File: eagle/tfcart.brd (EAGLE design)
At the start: 71.9 x 55.5 mm, 19 parts, among them CN1 MSX_CART, IC7 AT27C020-55JUPLCCS32, IC8 LM1117MPX-3.3

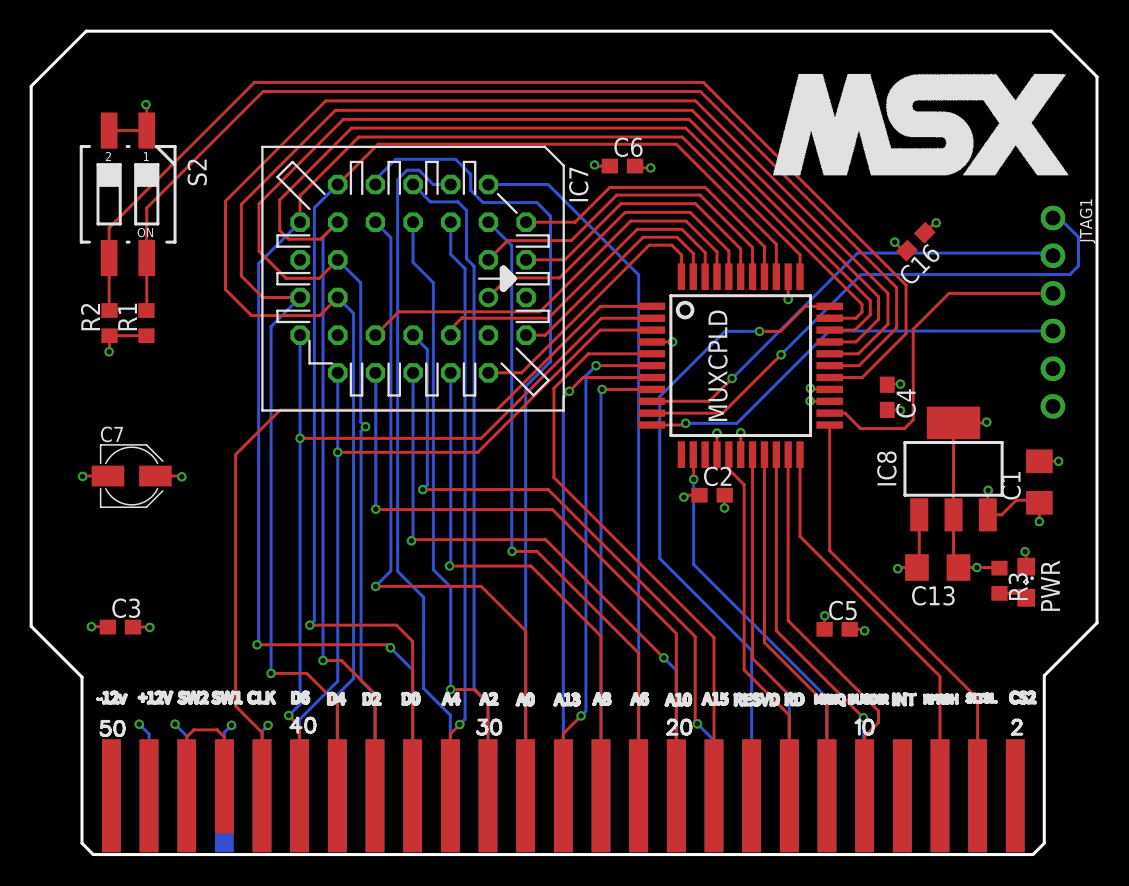
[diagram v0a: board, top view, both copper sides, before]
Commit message: MSX Cartridge v1.0 - Complete CPLD-based MegaROM implementation
A minimalist MSX cartridge design based on Xilinx XC9536XL CPLD with
complete build automation and manufacturing outputs.

NOTE: This project has been superseded by RISKYMSX. For new builds,
please use https://github.com/arkadiuszmakarenko/RISKYMSX which offers
superior features including USB ROM loading, SCC emulation, and better
user experience.

Features:
- Xilinx XC9536XL CPLD implementing standard MegaROM mapper
- 4 switchable ROM pages (8KB each) for up to 512KB ROMs
- Docker-based automated build system
- Complete PCB manufacturing pipeline (Gerbers, BOM, CPL, PDF)
- GitHub Actions CI/CD workflows
- GPL v3 licensed hardware and HDL

Build System:
- Docker containers for reproducible builds
- Automated firmware compilation with git versioning
- Eagle CAM processing for PCB manufacturing
- BOM/CPL extraction for assembly
- Automated release packaging

GitHub Actions Workflows:
- Firmware build (CPLD synthesis)
- Gerber generation (PCB fabrication files)
- Assembly file generation (BOM and CPL)
- Schematic PDF generation
- Complete release packaging

Manufacturing:
- 4-layer PCB design optimized for JLCPCB
- Automated Gerber generation via Eagle CAM
- Python scripts for BOM/CPL extraction
- Complete documentation for assembly

License: GNU General Public License v3.0
Copyright (C) 2021-2025 Stephen J. Leary

Build system based on tf536_public project structure.
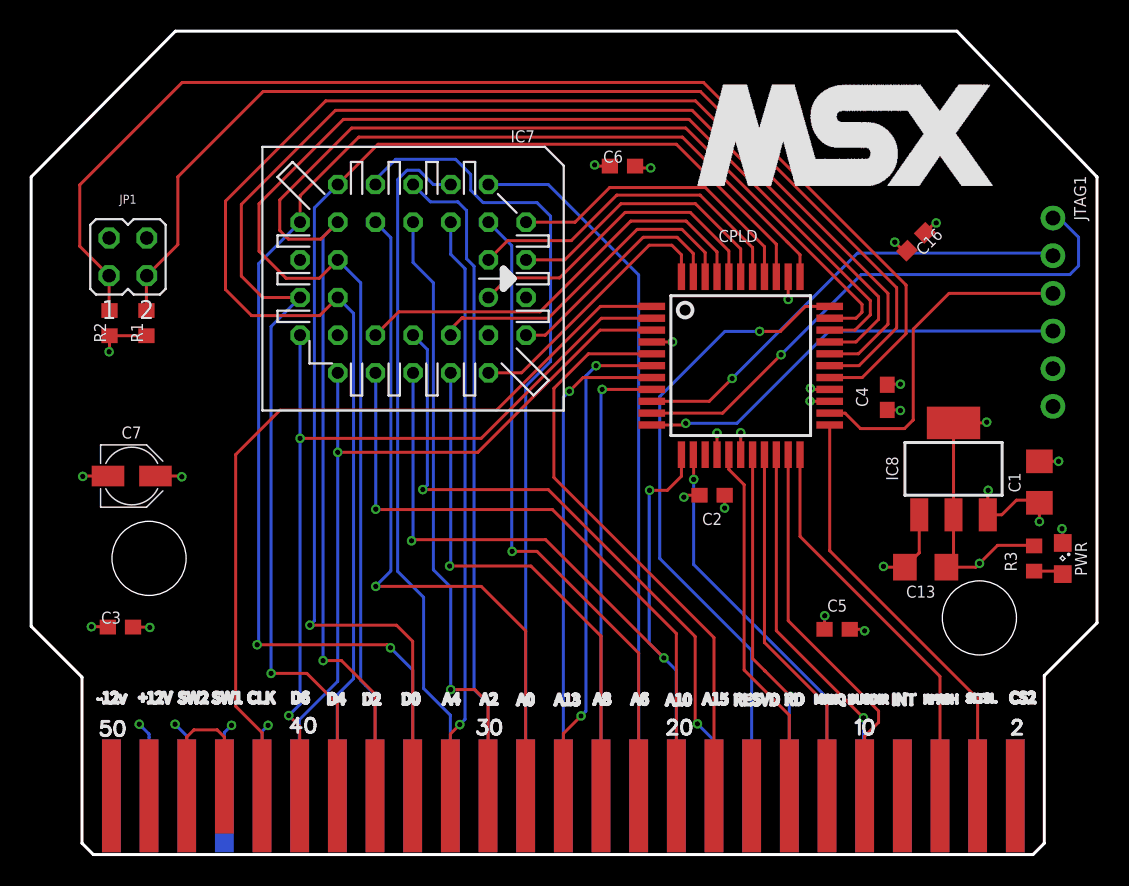
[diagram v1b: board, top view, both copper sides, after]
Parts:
- removed S2: 219-02, switch-dil:CTS-219-02
- added JP1: (no value), jumper:JP2Q
- CPLD: value XC9536_44VQ -> XC9536XL-10VQ44C
- moved PWR 2.94 mm to (66.2, 21.5)
- moved R3 2.78 mm to (64.3, 21.5)
- moved C13 0.81 mm to (56.9, 20.9)
- renumbered MUXCPLD to CPLD
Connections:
- net A11: now also CPLD.12
- net GND: now also JP1.2, JP1.4; no longer S2.1, S2.2
- net SW0: now also JP1.3; no longer S2.4
- net SW1: now also JP1.1; no longer S2.3
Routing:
- net A11: track 41.4 -> 57.1 mm, vias 2 -> 3
- net SW1: track 78.7 -> 83.2 mm
- net GND: track 33.5 -> 29.6 mm, vias 16 -> 15
- net VCC33: track 23.2 -> 27.0 mm
- net D3: track 100.0 -> 99.7 mm, vias 1 -> 0
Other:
- outline, holes or cut-outs redrawn
